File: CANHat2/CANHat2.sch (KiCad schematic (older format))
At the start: 23 parts, among them J0 RPi_GPIO, J1 SPI Select, J2 PWR Select, J3 RJ45, J4 RJ45, J5 Termination, T1 12 Volts, U1 MCP2515, U2 ISO1050DUB, U3 LM78L05ACZ, X1 8 MHz

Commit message: Update part numbers for CANHat2
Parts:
- C1: Mouser Part Number (none) -> 667-ECA-1HM100I
- C2, C4: Mouser Part Number (none) -> 594-K220J10C0GF5UH5
- C3, C6: Mouser Part Number (none) -> 21RZ310-RC
- C5: Mouser Part Number (none) -> 75-1C10Z5U334M050B
- C7: Mouser Part Number (none) -> 75-1C10Z5U473M050B
- D1, D2: Mouser Part Number (none) -> 771-BAT86133
- J0: Adafruit  (none) -> 2223; Mouser Part Number (none) -> 855-M20-6102045
- J1, J2: Mouser Part Number (none) -> 538-22-28-8034
- J3, J4: Mouser Part Number (none) -> 592-RJ45-8N-S
- J5: Mouser Part Number (none) -> 649-67997-404HLF
- R1: Mouser Part Number (none) -> 603-CFR-25JR-5210K
- R2, R3: Mouser Part Number (none) -> 71-RN60C60R0B/R
- T1: Mouser Part Number (none) -> 571-1776118-2
- U1: footprint DIL-18_300 -> DIP-18_300; Mouser Part Number (none) -> 579-MCP2515-I/P
- U2: Mouser Part Number (none) -> 595-ISO1050DUBR
- U3: Mouser Part Number (none) -> 512-LM78L05ACZ
- X1: Mouser Part Number (none) -> 449-LFXTAL031818BULK
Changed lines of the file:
@@
 LIBS:valves
+LIBS:CANHat2-cache
 LIBS:CANHat2-cache
 EELAYER 27 0
@@
 Sheet 1 1
 Title ""
-Date "10 oct 2017"
+Date "15 oct 2017"
 Rev ""
 Comp ""
@@
 F 2 "RPi_Hat:Pin_Header_Straight_2x20" H 1600 1450 60  0001 C CNN
 F 3 "" H 1600 1450 60  0000 C CNN
+F 4 "855-M20-6102045" H 1600 1450 60  0001 C CNN "Mouser Part Number"
+F 5 "2223" H 1600 1450 60  0001 C CNN "Adafruit "
 	1    1600 1450
 	1    0    0    -1
@@
 F 0 "U1" H 3200 4950 60  0000 C CNN
 F 1 "MCP2515" H 3200 5350 60  0000 C CNN
-F 2 "DIL-18_300" H 3100 5150 60  0001 C CNN
+F 2 "DIP-18_300" H 3100 5150 60  0001 C CNN
 F 3 "~" H 3200 5250 60  0000 C CNN
+F 4 "579-MCP2515-I/P" H 3200 5250 60  0001 C CNN "Mouser Part Number"
 	1    3200 5250
 	1    0    0    -1
@@
 F 2 "~" H 2000 6300 60  0000 C CNN
 F 3 "~" H 2000 6300 60  0000 C CNN
+F 4 "449-LFXTAL031818BULK" H 2000 6300 60  0001 C CNN "Mouser Part Number"
 	1    2000 6300
 	1    0    0    -1
@@
 F 2 "~" H 1738 6450 30  0000 C CNN
 F 3 "~" H 1700 6600 60  0000 C CNN
+F 4 "594-K220J10C0GF5UH5" H 1700 6600 60  0001 C CNN "Mouser Part Number"
 	1    1700 6600
 	1    0    0    -1
@@
 F 2 "~" H 2338 6500 30  0000 C CNN
 F 3 "~" H 2300 6650 60  0000 C CNN
+F 4 "594-K220J10C0GF5UH5" H 2300 6650 60  0001 C CNN "Mouser Part Number"
 	1    2300 6650
 	1    0    0    -1
@@
 F 2 "~" H 1838 4400 30  0000 C CNN
 F 3 "~" H 1800 4550 60  0000 C CNN
+F 4 "21RZ310-RC" H 1800 4550 60  0001 C CNN "Mouser Part Number"
 	1    1800 4550
 	1    0    0    -1
@@
 F 2 "~" H 1350 4550 60  0000 C CNN
 F 3 "~" H 1350 4550 60  0000 C CNN
+F 4 "667-ECA-1HM100I" H 1350 4550 60  0001 C CNN "Mouser Part Number"
 	1    1350 4550
 	1    0    0    -1
@@
 F 2 "~" V 2280 4600 30  0000 C CNN
 F 3 "~" H 2350 4600 30  0000 C CNN
+F 4 "603-CFR-25JR-5210K" V 2350 4600 60  0001 C CNN "Mouser Part Number"
 	1    2350 4600
 	1    0    0    -1
@@
 F 2 "~" H 1400 5200 60  0000 C CNN
 F 3 "~" H 1400 5200 60  0000 C CNN
+F 4 "538-22-28-8034" V 1400 5200 60  0001 C CNN "Mouser Part Number"
 	1    1400 5200
 	-1   0    0    -1
@@
 F 2 "~" H 5500 1500 60  0000 C CNN
 F 3 "~" H 5500 1500 60  0000 C CNN
+F 4 "771-BAT86133" H 5500 1500 60  0001 C CNN "Mouser Part Number"
 	1    5500 1500
 	0    1    1    0
@@
 F 2 "~" H 5600 1900 60  0000 C CNN
 F 3 "~" H 5600 1900 60  0000 C CNN
+F 4 "771-BAT86133" H 5600 1900 60  0001 C CNN "Mouser Part Number"
 	1    5600 1900
 	0    -1   1    0
@@
 F 2 "TO-92" H 6050 2700 30  0000 C CIN
 F 3 "~" H 6050 2600 60  0000 C CNN
+F 4 "512-LM78L05ACZ" H 6050 2600 60  0001 C CNN "Mouser Part Number"
 	1    6050 2600
 	1    0    0    -1
@@
 F 2 "" H 5950 5100 60  0000 C CNN
 F 3 "" H 5950 5100 60  0000 C CNN
+F 4 "595-ISO1050DUBR" H 5950 5100 60  0001 C CNN "Mouser Part Number"
 	1    5950 5100
 	1    0    0    -1
@@
 F 2 "~" H 9600 2300 60  0000 C CNN
 F 3 "~" H 9600 2300 60  0000 C CNN
+F 4 "592-RJ45-8N-S" H 9600 2300 60  0001 C CNN "Mouser Part Number"
 	1    9600 2300
 	0    1    1    0
@@
 F 2 "~" H 9600 4150 60  0000 C CNN
 F 3 "~" H 9600 4150 60  0000 C CNN
+F 4 "592-RJ45-8N-S" H 9600 4150 60  0001 C CNN "Mouser Part Number"
 	1    9600 4150
 	0    1    1    0
@@
 F 2 "~" H 5538 2600 30  0000 C CNN
 F 3 "~" H 5500 2750 60  0000 C CNN
+F 4 "75-1C10Z5U334M050B" H 5500 2750 60  0001 C CNN "Mouser Part Number"
 	1    5500 2750
 	1    0    0    -1
@@
 F 2 "~" H 6638 2600 30  0000 C CNN
 F 3 "~" H 6600 2750 60  0000 C CNN
+F 4 "21RZ310-RC" H 6600 2750 60  0001 C CNN "Mouser Part Number"
 	1    6600 2750
 	1    0    0    -1
@@
 F 2 "~" H 5600 950 60  0000 C CNN
 F 3 "~" H 5600 950 60  0000 C CNN
+F 4 "571-1776118-2" V 5600 950 60  0001 C CNN "Mouser Part Number"
 	1    5600 950
 	0    -1   -1   0
@@
 F 2 "~" H 7000 3750 60  0000 C CNN
 F 3 "~" H 7000 3750 60  0000 C CNN
+F 4 "538-22-28-8034" V 7000 3750 60  0001 C CNN "Mouser Part Number"
 	1    7000 3750
 	1    0    0    -1
@@
 F 2 "~" H 7650 5900 60  0000 C CNN
 F 3 "~" H 7650 5900 60  0000 C CNN
+F 4 "649-67997-404HLF" H 7650 5900 60  0001 C CNN "Mouser Part Number"
 	1    7650 5900
 	1    0    0    -1
@@
 F 2 "~" V 7980 5500 30  0000 C CNN
 F 3 "~" H 8050 5500 30  0000 C CNN
+F 4 "71-RN60C60R0B/R" V 8050 5500 60  0001 C CNN "Mouser Part Number"
 	1    8050 5500
 	1    0    0    -1
@@
 F 2 "~" V 7180 5550 30  0000 C CNN
 F 3 "~" H 7250 5550 30  0000 C CNN
+F 4 "71-RN60C60R0B/R" V 7250 5550 60  0001 C CNN "Mouser Part Number"
 	1    7250 5550
 	1    0    0    -1
@@
 F 2 "~" H 8088 6300 30  0000 C CNN
 F 3 "~" H 8050 6450 60  0000 C CNN
+F 4 "75-1C10Z5U473M050B" H 8050 6450 60  0001 C CNN "Mouser Part Number"
 	1    8050 6450
 	1    0    0    -1

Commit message: Update CANHat2 to use cheaper non-filtered RJ45 connectors
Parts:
- J3, J4: Mouser Part Number 592-RJ45-8N-S -> 710-615008144221
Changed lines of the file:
@@
 Sheet 1 1
 Title ""
-Date "15 oct 2017"
+Date "18 feb 2018"
 Rev ""
 Comp ""
@@
 F 2 "~" H 9600 2300 60  0000 C CNN
 F 3 "~" H 9600 2300 60  0000 C CNN
-F 4 "592-RJ45-8N-S" H 9600 2300 60  0001 C CNN "Mouser Part Number"
+F 4 "710-615008144221" H 9600 2300 60  0001 C CNN "Mouser Part Number"
 	1    9600 2300
 	0    1    1    0
@@
 F 2 "~" H 9600 4150 60  0000 C CNN
 F 3 "~" H 9600 4150 60  0000 C CNN
-F 4 "592-RJ45-8N-S" H 9600 4150 60  0001 C CNN "Mouser Part Number"
+F 4 "710-615008144221" H 9600 4150 60  0001 C CNN "Mouser Part Number"
 	1    9600 4150
 	0    1    1    0

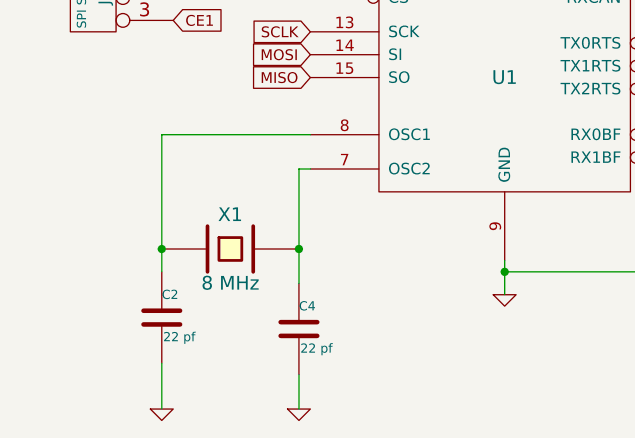
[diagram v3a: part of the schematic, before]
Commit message: Update to use a 16 mhz cyrstal
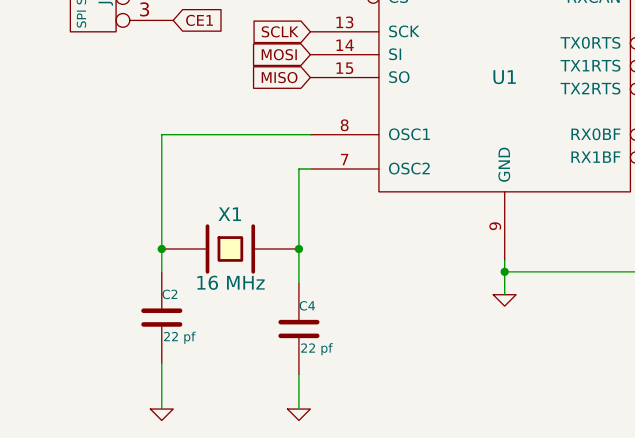
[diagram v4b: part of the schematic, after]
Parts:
- X1: value 8 MHz -> 16 MHz; Mouser Part Number 449-LFXTAL031818BULK -> 449-LFXTAL027945BULK
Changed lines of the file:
@@
 P 2000 6300
 F 0 "X1" H 2000 6450 60  0000 C CNN
-F 1 "8 MHz" H 2000 6150 60  0000 C CNN
+F 1 "16 MHz" H 2000 6150 60  0000 C CNN
 F 2 "~" H 2000 6300 60  0000 C CNN
 F 3 "~" H 2000 6300 60  0000 C CNN
-F 4 "449-LFXTAL031818BULK" H 2000 6300 60  0001 C CNN "Mouser Part Number"
+F 4 "449-LFXTAL027945BULK" H 2000 6300 60  0001 C CNN "Mouser Part Number"
 	1    2000 6300
 	1    0    0    -1
